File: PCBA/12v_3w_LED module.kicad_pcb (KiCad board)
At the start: 2 copper layers, 9 parts, among them P1 Generic Pad, P2 Generic Pad, P3 Generic Pad, U1 NCR321ZX

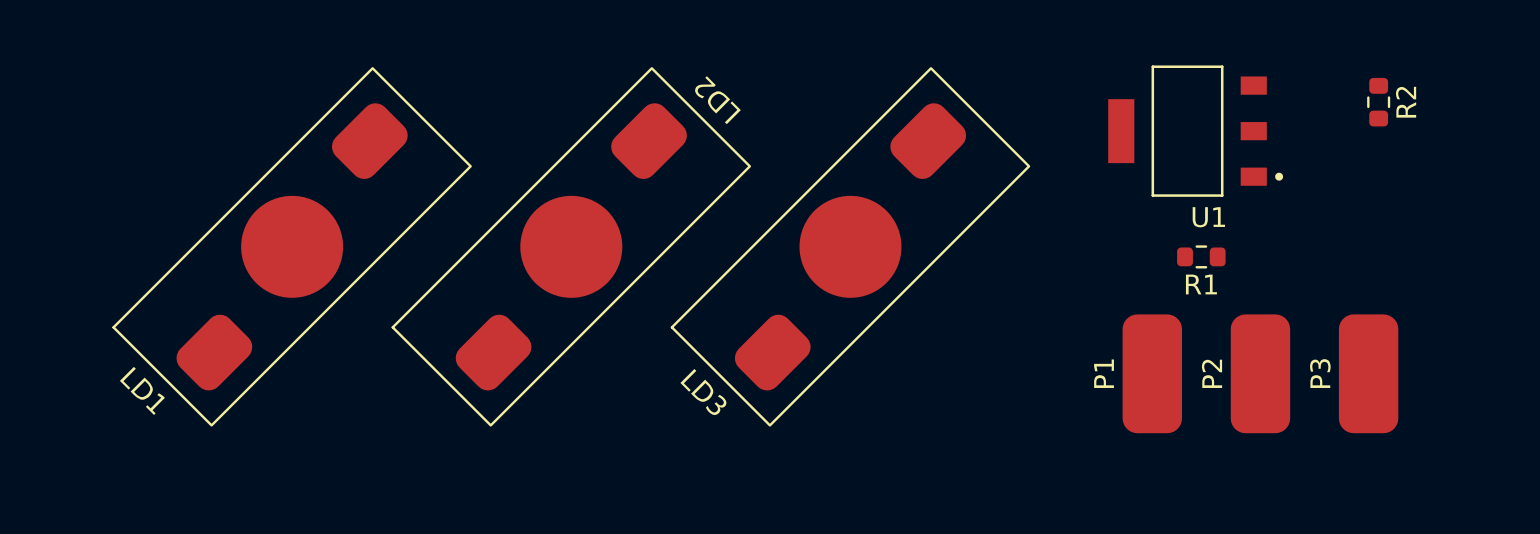
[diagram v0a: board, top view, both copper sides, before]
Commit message: completado el diseño de PCB
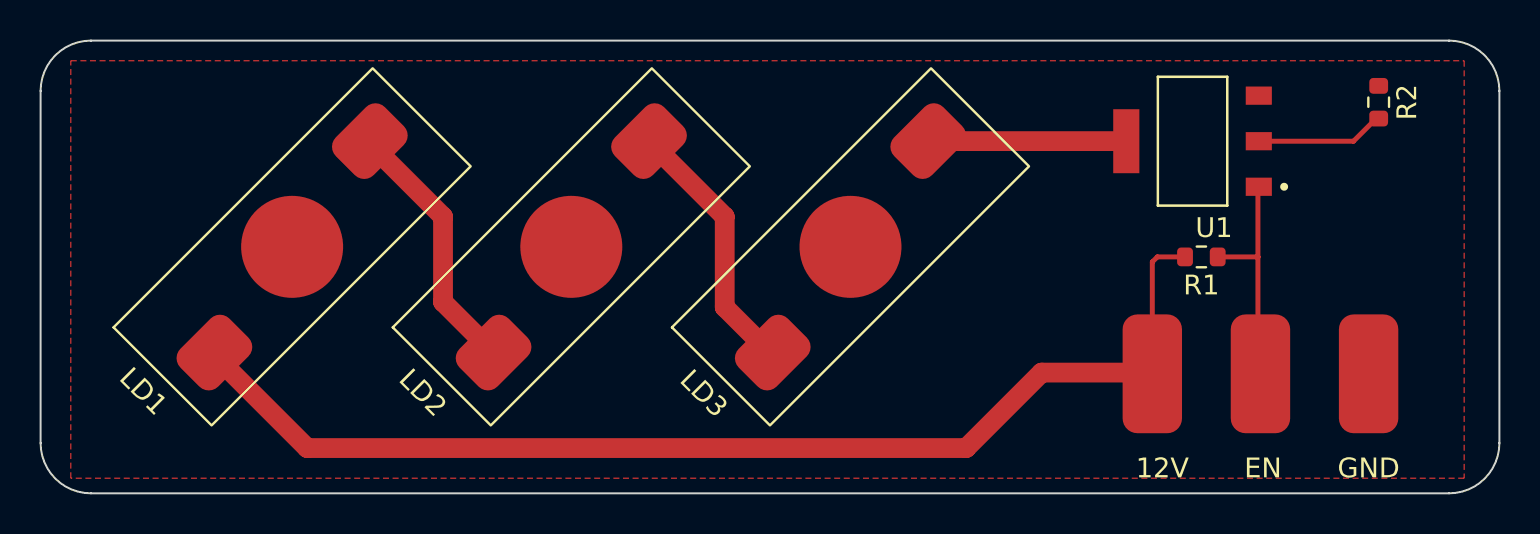
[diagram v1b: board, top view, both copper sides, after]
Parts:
- moved U1 0.57 mm to (182.6, 124.5)
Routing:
- net Net-(P1-Pad1): track 0.00 -> 58.4 mm
- net Net-(LD2-Pad2): track 0.00 -> 13.3 mm
- net Net-(LD1-Pad2): track 0.00 -> 13.3 mm
- net Net-(P2-Pad1): track 0.00 -> 11.6 mm
- net Net-(LD3-Pad2): track 0.00 -> 9.75 mm
- net Net-(R2-Pad2): track 0.00 -> 6.53 mm
- added copper zone on F.Cu, net Net-(P3-Pad1)
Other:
- board outline added: 73.7 x 22.9 mm
- board text added: "12V"
- board text added: "EN"
- board text added: "GND"
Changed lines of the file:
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@@
   )
   (footprint "Herranz - LED controller:SOT230P700X180-4N" (layer "F.Cu")
-    (at 182.372 123.952 180)
+    (at 182.626 124.46 180)
     (property "Sheetfile" "12v_3w_LED module.kicad_sch")
     (property "Sheetname" "")
@@
     (property "Voltage" "?V?")
     (attr smd)
-    (fp_text reference "P1" (at 0 -2.4 90 unlocked) (layer "F.SilkS")
+    (fp_text reference "P1" (at 0 -2.4 90 unlocked) (layer "F.SilkS") hide
       (effects (font (size 1 1) (thickness 0.15)))
     )
@@
     (property "Sheetname" "")
     (attr smd)
-    (fp_text reference "LD2" (at 10.47 -0.04 135 unlocked) (layer "F.SilkS")
+    (fp_text reference "LD2" (at -10.5069 -0.089803 315 unlocked) (layer "F.SilkS")
       (effects (font (size 1 1) (thickness 0.15)))
     )
@@
     (property "Voltage" "?V?")
     (attr smd)
-    (fp_text reference "P3" (at 0 -2.4 90 unlocked) (layer "F.SilkS")
+    (fp_text reference "P3" (at 0 -2.4 90 unlocked) (layer "F.SilkS") hide
       (effects (font (size 1 1) (thickness 0.15)))
     )
@@
     (property "Voltage" "?V?")
     (attr smd)
-    (fp_text reference "P2" (at 0 -2.4 90 unlocked) (layer "F.SilkS")
+    (fp_text reference "P2" (at 0 -2.4 90 unlocked) (layer "F.SilkS") hide
       (effects (font (size 1 1) (thickness 0.15)))
     )
@@
     )
   )
-  (group "" (id 5a6fb186-74b4-4e7e-8fda-3045984f1bae)
-    (members
-      0c45290b-d76f-4c88-a4f6-10a6b4367d24
-      1e5a4a4f-7ec1-4d5e-aab0-77eebafcd5cd
-      c7d84f6e-a707-4ffd-8ab8-e4d824111c03
-    )
-  )
+  (gr_line (start 127 119.38) (end 195.58 119.38) (layer "Edge.Cuts") (width 0.1))
+  (gr_line (start 127 142.24) (end 195.58 142.24) (layer "Edge.Cuts") (width 0.1))
+  (gr_arc (start 124.46 121.92) (mid 125.203949 120.123949) (end 127 119.38) (layer "Edge.Cuts") (width 0.1))
+  (gr_line (start 124.46 139.7) (end 124.46 121.92) (layer "Edge.Cuts") (width 0.1))
+  (gr_arc (start 198.12 139.7) (mid 197.376051 141.496051) (end 195.58 142.24) (layer "Edge.Cuts") (width 0.1))
+  (gr_line (start 198.12 139.7) (end 198.12 121.92) (layer "Edge.Cuts") (width 0.1))
+  (gr_arc (start 127 142.24) (mid 125.203949 141.496051) (end 124.46 139.7) (layer "Edge.Cuts") (width 0.1))
+  (gr_arc (start 195.58 119.38) (mid 197.376051 120.123949) (end 198.12 121.92) (layer "Edge.Cuts") (width 0.1))
+  (gr_text "GND\n" (at 191.516 140.97) (layer "F.SilkS")
+    (effects (font (size 1 1) (thickness 0.2)))
+  )
+  (gr_text "EN\n" (at 186.182 140.97) (layer "F.SilkS")
+    (effects (font (size 1 1) (thickness 0.2)))
+  )
+  (gr_text "12V " (at 181.102 140.97) (layer "F.SilkS")
+    (effects (font (size 1 1) (thickness 0.2)))
+  )
+  (segment (start 182.246 130.302) (end 180.848 130.302) (width 0.25) (layer "F.Cu") (net 1))
+  (segment (start 171.196 139.954) (end 175.006 136.144) (width 1) (layer "F.Cu") (net 1))
+  (segment (start 180.848 130.302) (end 180.594 130.556) (width 0.25) (layer "F.Cu") (net 1))
+  (segment (start 175.006 136.144) (end 180.532758 136.144) (width 1) (layer "F.Cu") (net 1))
+  (segment (start 180.594 130.556) (end 180.594 136.205242) (width 0.25) (layer "F.Cu") (net 1))
+  (segment (start 137.922 139.954) (end 171.196 139.954) (width 1) (layer "F.Cu") (net 1))
+  (segment (start 180.532758 136.144) (end 180.594 136.205242) (width 1) (layer "F.Cu") (net 1))
+  (segment (start 133.235557 135.267557) (end 137.922 139.954) (width 1) (layer "F.Cu") (net 1))
+  (segment (start 133.235557 135.132656) (end 133.235557 135.267557) (width 1) (layer "F.Cu") (net 1))
+  (segment (start 183.896 130.302) (end 185.928 130.302) (width 0.25) (layer "F.Cu") (net 2))
+  (segment (start 185.717 135.867242) (end 186.055 136.205242) (width 0.25) (layer "F.Cu") (net 2))
+  (segment (start 185.928 126.76) (end 185.928 130.302) (width 0.25) (layer "F.Cu") (net 2))
+  (segment (start 185.928 130.302) (end 185.928 135.867242) (width 0.25) (layer "F.Cu") (net 2))
+  (segment (start 141.084443 124.455344) (end 141.084443 124.574443) (width 1) (layer "F.Cu") (net 4))
+  (segment (start 144.78 132.580099) (end 147.332557 135.132656) (width 1) (layer "F.Cu") (net 4))
+  (segment (start 141.084443 124.574443) (end 144.78 128.27) (width 1) (layer "F.Cu") (net 4))
+  (segment (start 144.78 128.27) (end 144.78 132.580099) (width 1) (layer "F.Cu") (net 4))
+  (segment (start 190.754 124.46) (end 191.898 123.316) (width 0.25) (layer "F.Cu") (net 5))
+  (segment (start 191.898 123.316) (end 192.024 123.316) (width 0.25) (layer "F.Cu") (net 5))
+  (segment (start 185.971 124.46) (end 190.754 124.46) (width 0.25) (layer "F.Cu") (net 5))
+  (segment (start 161.294656 135.132656) (end 161.429557 135.132656) (width 1) (layer "F.Cu") (net 6))
+  (segment (start 155.189344 124.455344) (end 159.004 128.27) (width 1) (layer "F.Cu") (net 6))
+  (segment (start 159.004 132.842) (end 161.294656 135.132656) (width 1) (layer "F.Cu") (net 6))
+  (segment (start 155.181443 124.455344) (end 155.189344 124.455344) (width 1) (layer "F.Cu") (net 6))
+  (segment (start 159.004 128.27) (end 159.004 132.842) (width 1) (layer "F.Cu") (net 6))
+  (segment (start 179.022344 124.455344) (end 179.027 124.46) (width 1) (layer "F.Cu") (net 7))
+  (segment (start 169.278443 124.455344) (end 179.022344 124.455344) (width 1) (layer "F.Cu") (net 7))
+  (zone (net 3) (net_name "Net-(P3-Pad1)") (layer "F.Cu") (hatch edge 0.508)
+    (connect_pads (clearance 0.508))
+    (min_thickness 0.254) (filled_areas_thickness no)
+    (fill yes (thermal_gap 0.508) (thermal_bridge_width 1))
+    (polygon
+      (pts
+        (xy 196.342 141.478)
+        (xy 125.984 141.478)
+        (xy 125.984 120.396)
+        (xy 196.342 120.396)
+      )
+    )
+  )
